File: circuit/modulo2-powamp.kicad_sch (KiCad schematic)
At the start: 77 parts, among them J1 HOLE, J2 HOLE, J3 HOLE, J4 HOLE, J5 CONN_01X04, J6 CONN_01X04, SW1 reset, SW2 mute, SW3 HEAD/AD, U1 LM1117-5.0, U2 TPA3220, U3 MCP16331

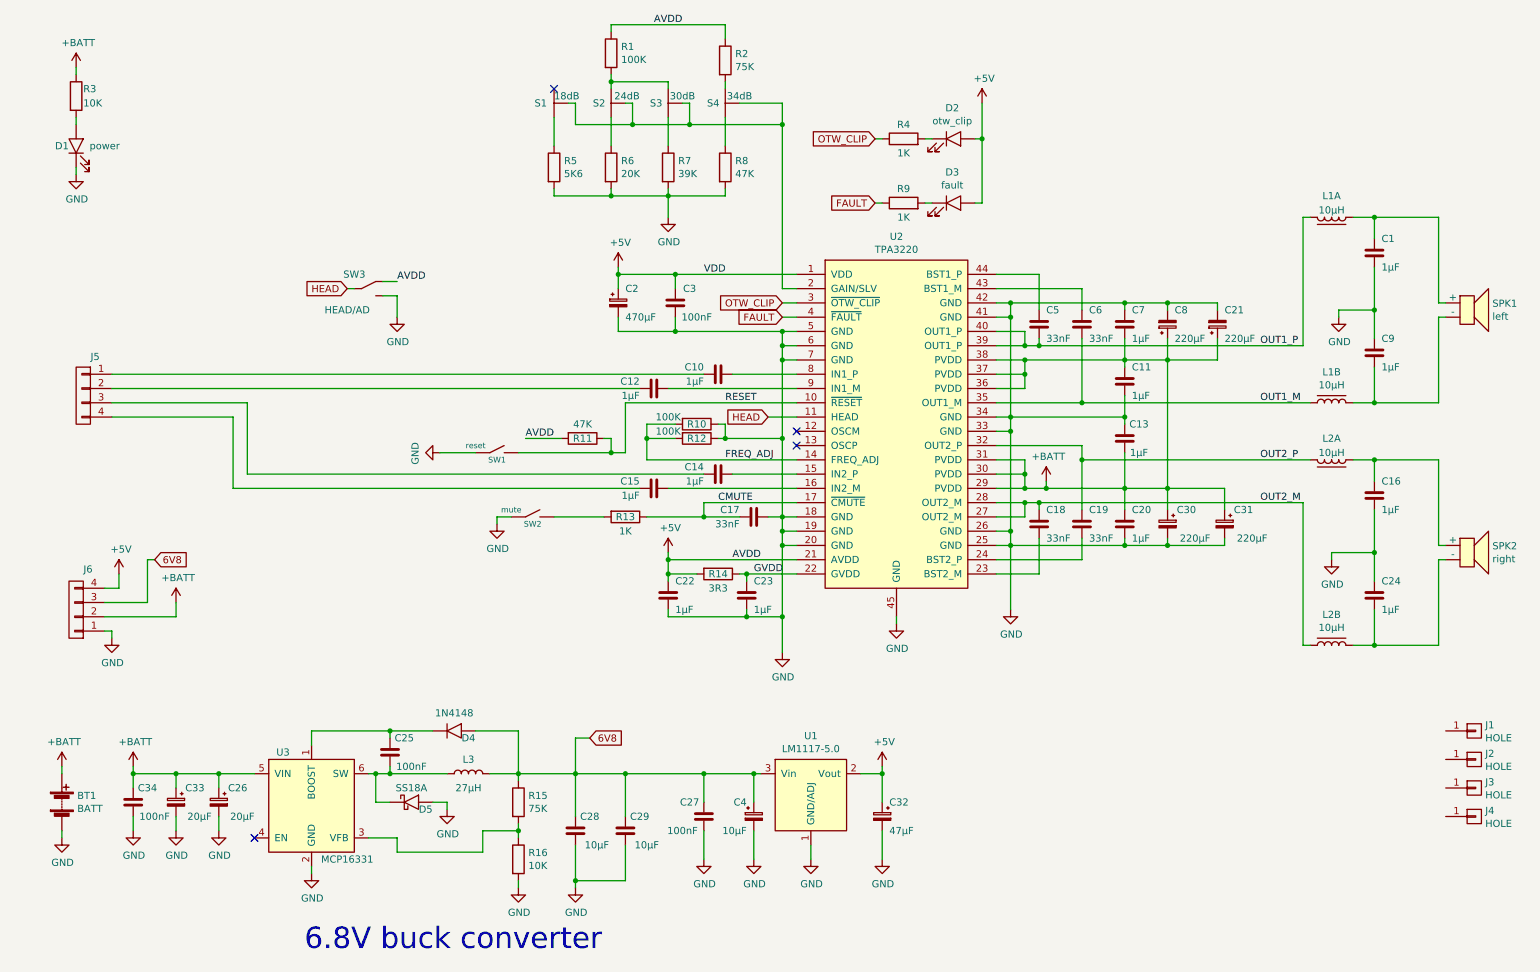
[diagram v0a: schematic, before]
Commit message: added report on createBanks.py; started PCB redesign
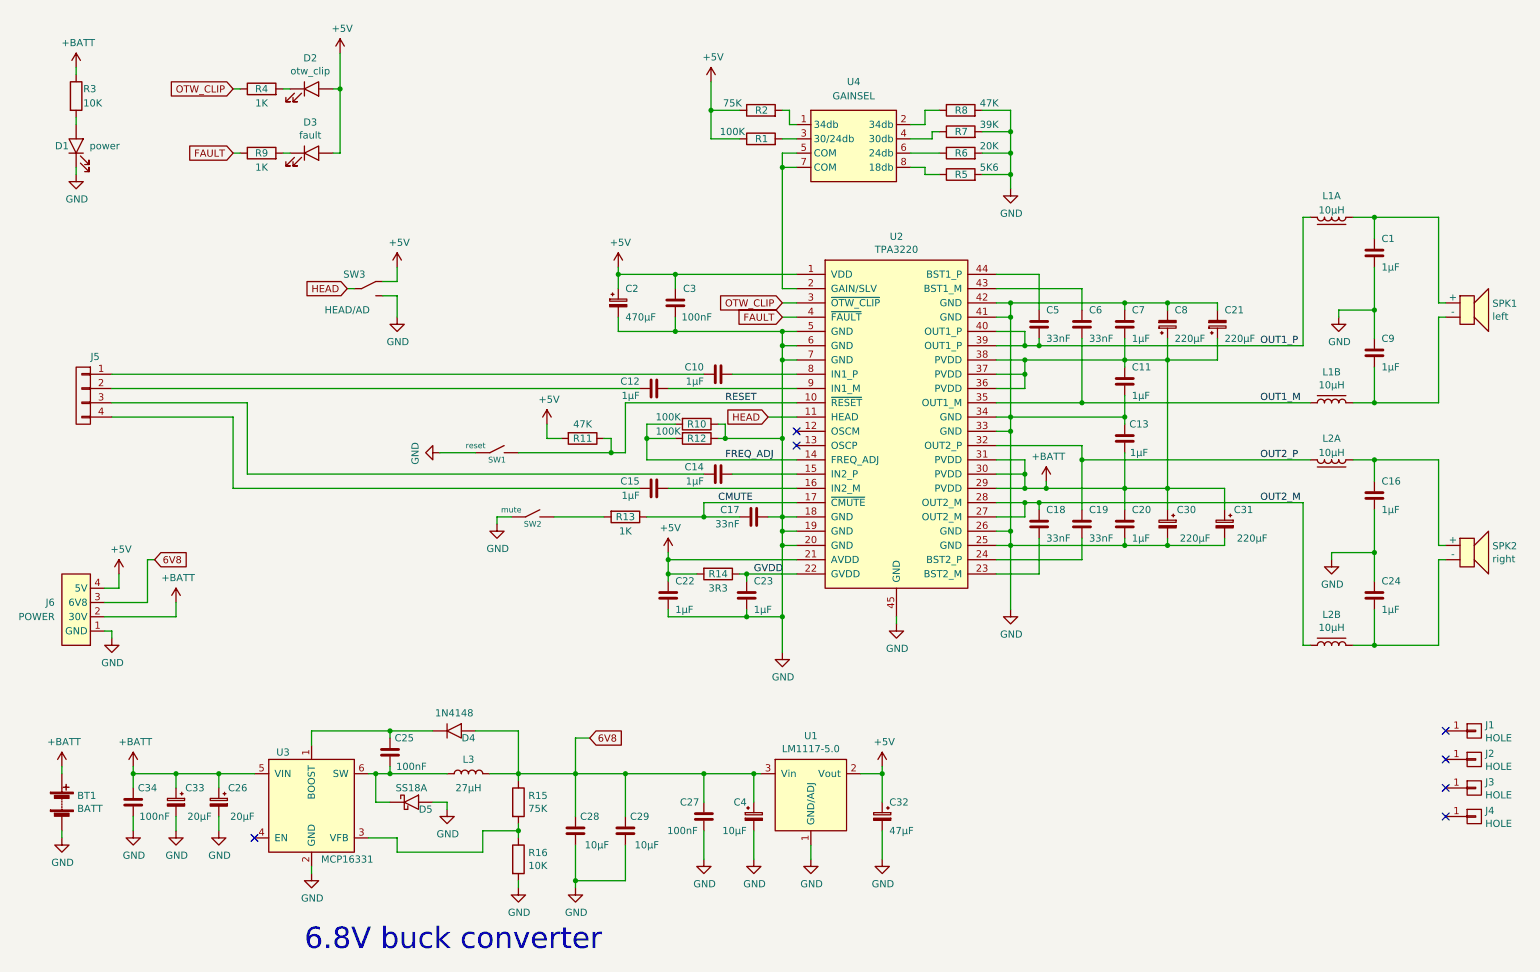
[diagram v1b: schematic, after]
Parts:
- removed J6: CONN_01X04, myAmp:PIN_1x04, symbol myAmp:CONN_01X04
- removed S1: 18dB, myAmp:JUMPER_3WAY, symbol myAmp:JUMPER_3WAY
- removed S2: 24dB, myAmp:JUMPER_3WAY, symbol myAmp:JUMPER_3WAY
- removed S3: 30dB, myAmp:JUMPER_3WAY, symbol myAmp:JUMPER_3WAY
- removed S4: 34dB, myAmp:JUMPER_3WAY, symbol myAmp:JUMPER_3WAY
- added J6: POWER, myAmp:POWER, symbol myAmp:POWER
- added U4: GAINSEL, myAmp:GAINSEL, symbol myAmp:GAINSEL
- C1, C10, C12, C14, C15, C16, C24, C9: footprint myAmp:C_FILM_L7.2mm_W4.5mm_P5.00mm -> myAmp:C_FILM_L7.2mm_W5.0mm_P5.00mm
- D4: footprint myAmp:D_SOD-123 -> myAmp:DO35
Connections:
- net +5V: now also J6.4 (5V)
- net +BATT: now also J6.2 (30V)
- net 6V8: now also J6.3 (6V8)
- net GND: now also J6.1 (GND)
- net at U2.2 (GAIN/SLV): now also U4.5 (COM), U4.7 (COM)
- net at R5.1: now also U4.8 (18db)
- net at R1.2: now also U4.3 (30/24db)
- net at R6.1: now also U4.6 (24db)
- net at R2.2: now also U4.1 (34db)
- net at R7.1: now also U4.4 (30db)
- net at R8.1: now also U4.2 (34db)
- no-connect marks 4 -> 7
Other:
- moved on the sheet: D2, D3, R1, R2, R4, R5, R6, R7, R8, R9

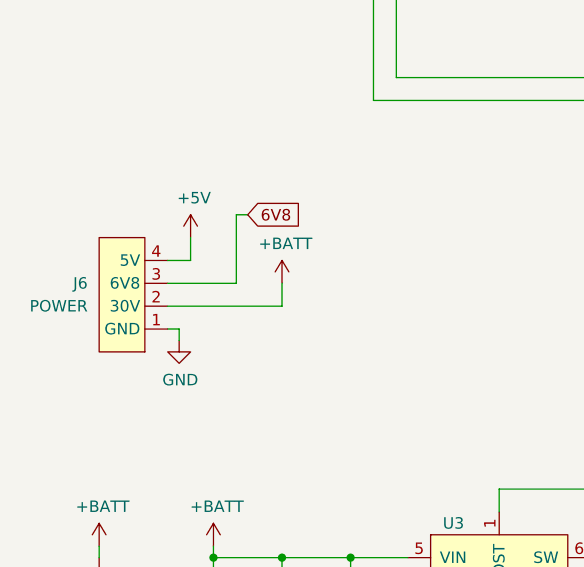
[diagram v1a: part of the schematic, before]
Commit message: no more assembler; more routing
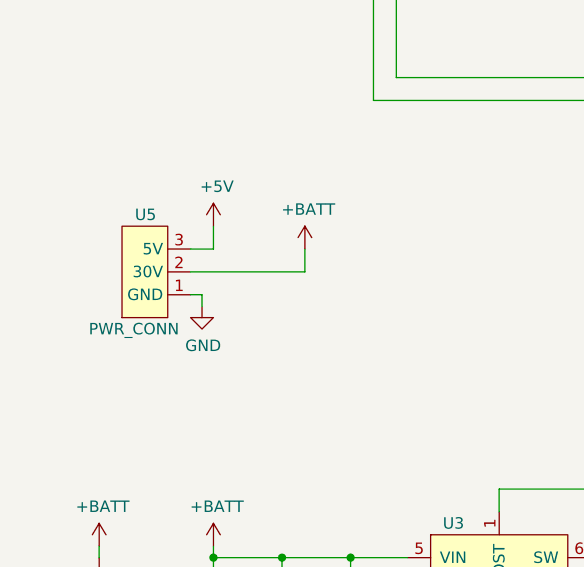
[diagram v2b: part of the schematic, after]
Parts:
- removed J6: POWER, myAmp:POWER, symbol myAmp:POWER
- added U5: PWR_CONN, myAmp:PWR_CONN, symbol myAmp:PWR_CONN
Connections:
- net +5V: now also U5.3 (5V)
- net +BATT: now also U5.2 (30V)
- net GND: now also U5.1 (GND)
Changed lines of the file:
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@@
     (stroke (width 0) (type default) (color 0 0 0 0))
   )
-  (wire (pts (xy 30.48 124.46) (xy 43.18 124.46))
+  (wire (pts (xy 33.02 120.65) (xy 45.72 120.65))
     (stroke (width 0) (type default) (color 0 0 0 0))
   )
@@
     (stroke (width 0) (type default) (color 0 0 0 0))
   )
-  (wire (pts (xy 30.48 127) (xy 31.75 127))
-    (stroke (width 0) (type default) (color 0 0 0 0))
-  )
-  (wire (pts (xy 31.75 127) (xy 31.75 128.27))
+  (wire (pts (xy 33.02 123.19) (xy 34.29 123.19))
+    (stroke (width 0) (type default) (color 0 0 0 0))
+  )
+  (wire (pts (xy 34.29 123.19) (xy 34.29 124.46))
     (stroke (width 0) (type default) (color 0 0 0 0))
   )
@@
     (stroke (width 0) (type default) (color 0 0 0 0))
   )
-  (wire (pts (xy 38.1 114.3) (xy 38.1 121.92))
-    (stroke (width 0) (type default) (color 0 0 0 0))
-  )
   (wire (pts (xy 121.92 62.23) (xy 121.92 63.5))
     (stroke (width 0) (type default) (color 0 0 0 0))
@@
     (stroke (width 0) (type default) (color 0 0 0 0))
   )
-  (wire (pts (xy 39.37 114.3) (xy 38.1 114.3))
-    (stroke (width 0) (type default) (color 0 0 0 0))
-  )
   (wire (pts (xy 67.31 147.32) (xy 67.31 144.78))
     (stroke (width 0) (type default) (color 0 0 0 0))
@@
     (stroke (width 0) (type default) (color 0 0 0 0))
   )
-  (wire (pts (xy 43.18 121.92) (xy 43.18 124.46))
+  (wire (pts (xy 45.72 118.11) (xy 45.72 120.65))
     (stroke (width 0) (type default) (color 0 0 0 0))
   )
@@
     (stroke (width 0) (type default) (color 0 0 0 0))
   )
-  (wire (pts (xy 38.1 121.92) (xy 30.48 121.92))
-    (stroke (width 0) (type default) (color 0 0 0 0))
-  )
   (wire (pts (xy 151.13 39.37) (xy 153.67 39.37))
     (stroke (width 0) (type default) (color 0 0 0 0))
@@
     (stroke (width 0) (type default) (color 0 0 0 0))
   )
-  (wire (pts (xy 30.48 119.38) (xy 33.02 119.38))
+  (wire (pts (xy 33.02 118.11) (xy 35.56 118.11))
     (stroke (width 0) (type default) (color 0 0 0 0))
   )
@@
     (stroke (width 0) (type default) (color 0 0 0 0))
   )
-  (wire (pts (xy 33.02 119.38) (xy 33.02 116.84))
+  (wire (pts (xy 35.56 118.11) (xy 35.56 115.57))
     (stroke (width 0) (type default) (color 0 0 0 0))
   )
@@
   (global_label "HEAD" (shape input) (at 73.66 66.04 180) (fields_autoplaced)
     (effects (font (size 1.27 1.27)) (justify right))
-    (property "Intersheet References" "${INTERSHEET_REFS}" (id 0) (at 0 0 0)
-      (effects (font (size 1.27 1.27)) hide)
-    )
-  )
-  (global_label "6V8" (shape input) (at 39.37 114.3 0) (fields_autoplaced)
-    (effects (font (size 1.27 1.27)) (justify left))
     (property "Intersheet References" "${INTERSHEET_REFS}" (id 0) (at 0 0 0)
       (effects (font (size 1.27 1.27)) hide)
@@
     (pin "2")
   )
-  (symbol (lib_id "power:GND") (at 31.75 128.27 0) (unit 1)
-    (in_bom yes) (on_board yes)
-    (property "Reference" "#PWR0103" (id 0) (at 31.75 134.62 0)
-      (effects (font (size 1.27 1.27)) hide)
-    )
-    (property "Value" "GND" (id 1) (at 31.877 132.6642 0))
-    (property "Footprint" "" (id 2) (at 31.75 128.27 0)
-      (effects (font (size 1.27 1.27)) hide)
-    )
-    (property "Datasheet" "" (id 3) (at 31.75 128.27 0)
+  (symbol (lib_id "power:GND") (at 34.29 124.46 0) (unit 1)
+    (in_bom yes) (on_board yes)
+    (property "Reference" "#PWR0103" (id 0) (at 34.29 130.81 0)
+      (effects (font (size 1.27 1.27)) hide)
+    )
+    (property "Value" "GND" (id 1) (at 34.417 128.8542 0))
+    (property "Footprint" "" (id 2) (at 34.29 124.46 0)
+      (effects (font (size 1.27 1.27)) hide)
+    )
+    (property "Datasheet" "" (id 3) (at 34.29 124.46 0)
       (effects (font (size 1.27 1.27)) hide)
     )
@@
     (pin "1")
   )
-  (symbol (lib_id "power:+BATT") (at 43.18 121.92 0) (unit 1)
-    (in_bom yes) (on_board yes)
-    (property "Reference" "#PWR0125" (id 0) (at 43.18 125.73 0)
-      (effects (font (size 1.27 1.27)) hide)
-    )
-    (property "Value" "+BATT" (id 1) (at 43.561 117.5258 0))
-    (property "Footprint" "" (id 2) (at 43.18 121.92 0)
-      (effects (font (size 1.27 1.27)) hide)
-    )
-    (property "Datasheet" "" (id 3) (at 43.18 121.92 0)
+  (symbol (lib_id "power:+BATT") (at 45.72 118.11 0) (unit 1)
+    (in_bom yes) (on_board yes)
+    (property "Reference" "#PWR0125" (id 0) (at 45.72 121.92 0)
+      (effects (font (size 1.27 1.27)) hide)
+    )
+    (property "Value" "+BATT" (id 1) (at 46.101 113.7158 0))
+    (property "Footprint" "" (id 2) (at 45.72 118.11 0)
+      (effects (font (size 1.27 1.27)) hide)
+    )
+    (property "Datasheet" "" (id 3) (at 45.72 118.11 0)
       (effects (font (size 1.27 1.27)) hide)
     )
@@
     (pin "1")
   )
-  (symbol (lib_id "power:+5V") (at 33.02 116.84 0) (unit 1)
-    (in_bom yes) (on_board yes)
-    (property "Reference" "#PWR0127" (id 0) (at 33.02 120.65 0)
-      (effects (font (size 1.27 1.27)) hide)
-    )
-    (property "Value" "+5V" (id 1) (at 33.401 112.4458 0))
-    (property "Footprint" "" (id 2) (at 33.02 116.84 0)
-      (effects (font (size 1.27 1.27)) hide)
-    )
-    (property "Datasheet" "" (id 3) (at 33.02 116.84 0)
+  (symbol (lib_id "power:+5V") (at 35.56 115.57 0) (unit 1)
+    (in_bom yes) (on_board yes)
+    (property "Reference" "#PWR0127" (id 0) (at 35.56 119.38 0)
+      (effects (font (size 1.27 1.27)) hide)
+    )
+    (property "Value" "+5V" (id 1) (at 35.941 111.1758 0))
+    (property "Footprint" "" (id 2) (at 35.56 115.57 0)
+      (effects (font (size 1.27 1.27)) hide)
+    )
+    (property "Datasheet" "" (id 3) (at 35.56 115.57 0)
       (effects (font (size 1.27 1.27)) hide)
     )
@@
     (pin "1")
   )
-  (symbol (lib_id "myAmp:POWER") (at 26.67 123.19 0) (mirror x) (unit 1)
-    (in_bom yes) (on_board yes) (fields_autoplaced)
-    (property "Reference" "J6" (id 0) (at 21.59 121.9199 0)
-      (effects (font (size 1.27 1.27)) (justify right))
-    )
-    (property "Value" "POWER" (id 1) (at 21.59 124.4599 0)
-      (effects (font (size 1.27 1.27)) (justify right))
-    )
-    (property "Footprint" "myAmp:POWER" (id 2) (at 29.21 123.19 0)
-      (effects (font (size 1.27 1.27)) hide)
-    )
-    (property "Datasheet" "" (id 3) (at 29.21 123.19 0)
-      (effects (font (size 1.27 1.27)) hide)
-    )
-    (pin "1")
-    (pin "2")
-    (pin "3")
-    (pin "4")
-  )
   (symbol (lib_id "power:+5V") (at 109.22 90.17 0) (unit 1)
     (in_bom yes) (on_board yes)
@@
     )
     (pin "1")
+  )
+  (symbol (lib_id "myAmp:PWR_CONN") (at 29.21 120.65 0) (mirror x) (unit 1)
+    (in_bom yes) (on_board yes)
+    (property "Reference" "U5" (id 0) (at 29.21 114.3 0)
+      (effects (font (size 1.27 1.27)) (justify right))
+    )
+    (property "Value" "PWR_CONN" (id 1) (at 31.75 127 0)
+      (effects (font (size 1.27 1.27)) (justify right))
+    )
+    (property "Footprint" "myAmp:PWR_CONN" (id 2) (at 31.75 119.38 0)
+      (effects (font (size 1.27 1.27)) hide)
+    )
+    (property "Datasheet" "" (id 3) (at 31.75 119.38 0)
+      (effects (font (size 1.27 1.27)) hide)
+    )
+    (pin "1")
+    (pin "2")
+    (pin "3")
   )
   (sheet_instances
@@
       (reference "J5") (unit 1) (value "CONN_01X04") (footprint "myAmp:PIN_1x04")
     )
-    (path "/c3934c43-993a-49df-98d8-248670a21859"
-      (reference "J6") (unit 1) (value "POWER") (footprint "myAmp:POWER")
-    )
     (path "/00000000-0000-0000-0000-00005c9cc63c"
       (reference "L1") (unit 1) (value "10μH") (footprint "myAmp:COILCRAFT-UA801x-AL")
@@
       (reference "U4") (unit 1) (value "GAINSEL") (footprint "myAmp:GAINSEL")
     )
-  )
+    (path "/fd01492a-3151-4387-b505-242e8460e58f"
+      (reference "U5") (unit 1) (value "PWR_CONN") (footprint "myAmp:PWR_CONN")
+    )
+  )

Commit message: getting closer to the final PCBs; still have to change the rotenc
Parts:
- removed SW2: mute, myAmp:Switch_2.5mm, symbol myAmp:SW_SIMPLE
- added Q1: BS170, myAmp:TO-92_Inline_Wide, symbol myAmp:NMOS
- added R17: 47K, myAmp:R_0805, symbol myAmp:R
- added U6: AMPCTRL, myAmp:PIN_1x03, symbol myAmp:AMPCTRL
- R10, R11, R12: footprint myAmp:R_0805 -> myAmp:R_10MM
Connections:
- net GND: now also Q1.3 (S), R17.2, U6.1 (GND)
- net RESET: now also U6.2 (RESET)
- net at R13.2: now also Q1.1 (D)
- new net: Q1.2 (G), R17.1, U6.3 (MUTE)

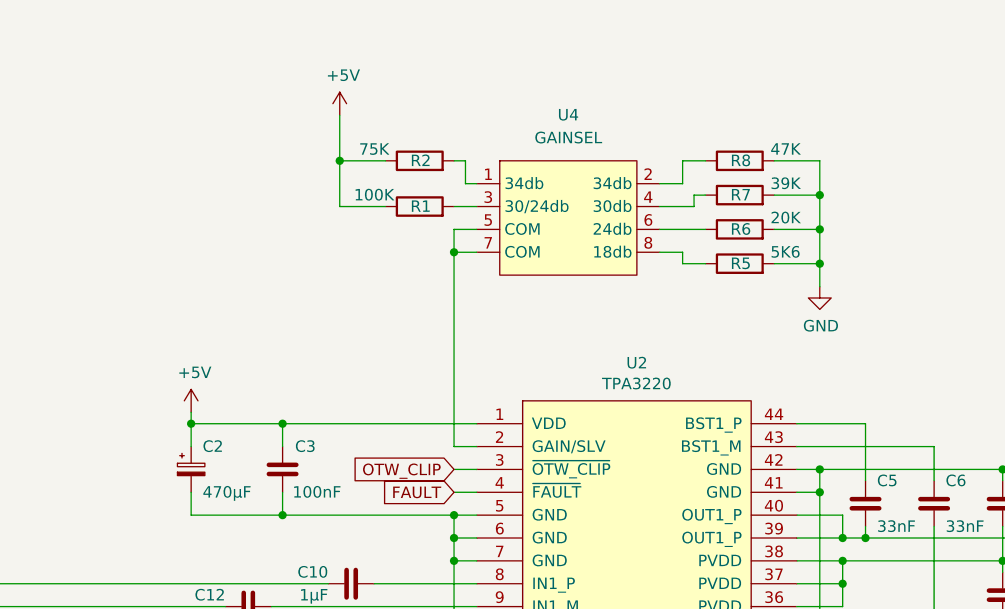
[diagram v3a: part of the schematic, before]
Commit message: found new switch for gain select; eq needs redesign
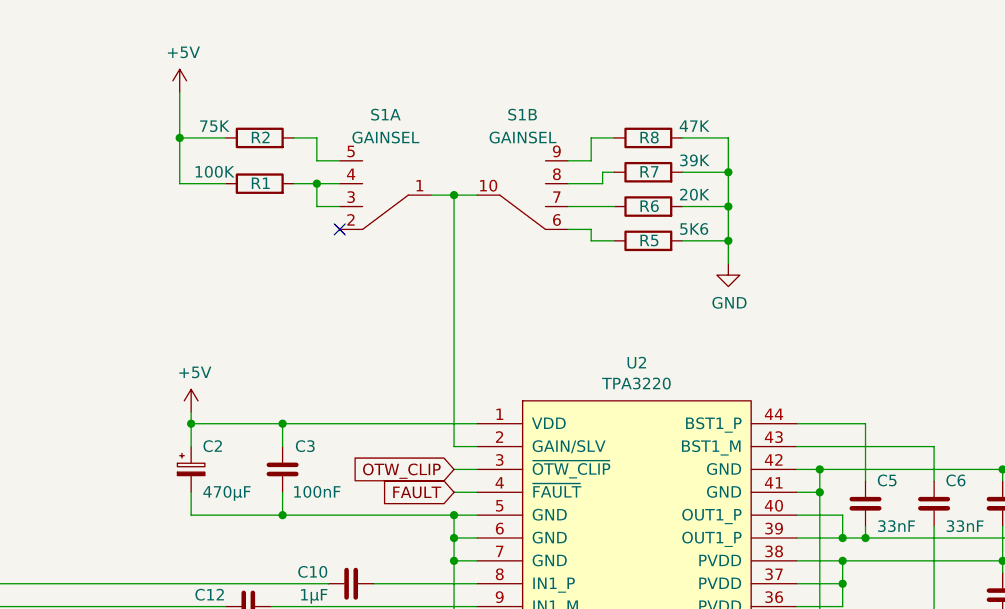
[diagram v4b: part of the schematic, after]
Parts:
- removed U4: GAINSEL, myAmp:GAINSEL, symbol myAmp:GAINSEL
- added S1: GAINSEL, myAmp:SR10010F-0204, symbol myAmp:SW_2P4T
- R10, R11, R12: footprint myAmp:R_10MM -> myAmp:R_0805
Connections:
- net at U2.2 (GAIN/SLV): now also S1.1, S1.10
- net at R5.1: now also S1.6
- net at R1.2: now also S1.3, S1.4
- net at R6.1: now also S1.7
- net at R2.2: now also S1.5
- net at R7.1: now also S1.8
- net at R8.1: now also S1.9
- no-connect marks 7 -> 8
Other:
- moved on the sheet: R1, R2, R5, R6, R7, R8

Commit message: ditched the LED array board; LEDs are on the main PCB now
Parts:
- C2: footprint myAmp:CPOL_D6.3_P2.5 -> myAmp:CPOL_D8_P3.5
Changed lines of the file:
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@@
       (effects (font (size 1.27 1.27)) (justify left))
     )
-    (property "Footprint" "myAmp:CPOL_D6.3_P2.5" (id 2) (at 121.92 68.58 0)
+    (property "Footprint" "myAmp:CPOL_D8_P3.5" (id 2) (at 121.92 68.58 0)
       (effects (font (size 1.27 1.27)) hide)
     )
@@
     )
     (path "/00000000-0000-0000-0000-00005c81ba70"
-      (reference "C2") (unit 1) (value "470μF") (footprint "myAmp:CPOL_D6.3_P2.5")
+      (reference "C2") (unit 1) (value "470μF") (footprint "myAmp:CPOL_D8_P3.5")
     )
     (path "/00000000-0000-0000-0000-00005c8cabce"
